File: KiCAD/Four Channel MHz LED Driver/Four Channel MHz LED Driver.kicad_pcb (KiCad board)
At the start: 2 copper layers, 100 x 100 mm, 89 parts, among them J1 Barrel_Jack_Switch, J10 Conn_01x08_Female, J2 Conn_01x02_Female, J3 8P8C_Shielded_x4, J4 Conn_01x05_Female, J5 Conn_01x24_Female, J6 Conn_01x03_Male, J7 Conn_01x24_Female, J8 Conn_01x03_Female, J9 Conn_01x03_Female, M1 Fan_4pin, Q2 SUM70060E, SW1 SW_SPDT, SW2 Pushbutton_with_LED_-_ELUMOAT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, SW3 Pushbutton_with_LED_-_ELUMOAT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, SW4 Pushbutton_with_LED_-_ELUMOAT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, SW5 Pushbutton_with_LED_-_ELUMOAT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, U1 12V boost, U10 LT6200CS8-10, U14 Teensy3.6, U16 SN74LV4T125PWR, U2 ASSR-1218, U3 DPBW06F-05, U4 BDJ0GA5WEFJ-E2, U5 ADP7182AUJZ-1.8-R7, U6 TMUX1204DGSR, U7 ASSR-1218, U8 ASSR-1218, U9 ASSR-1218

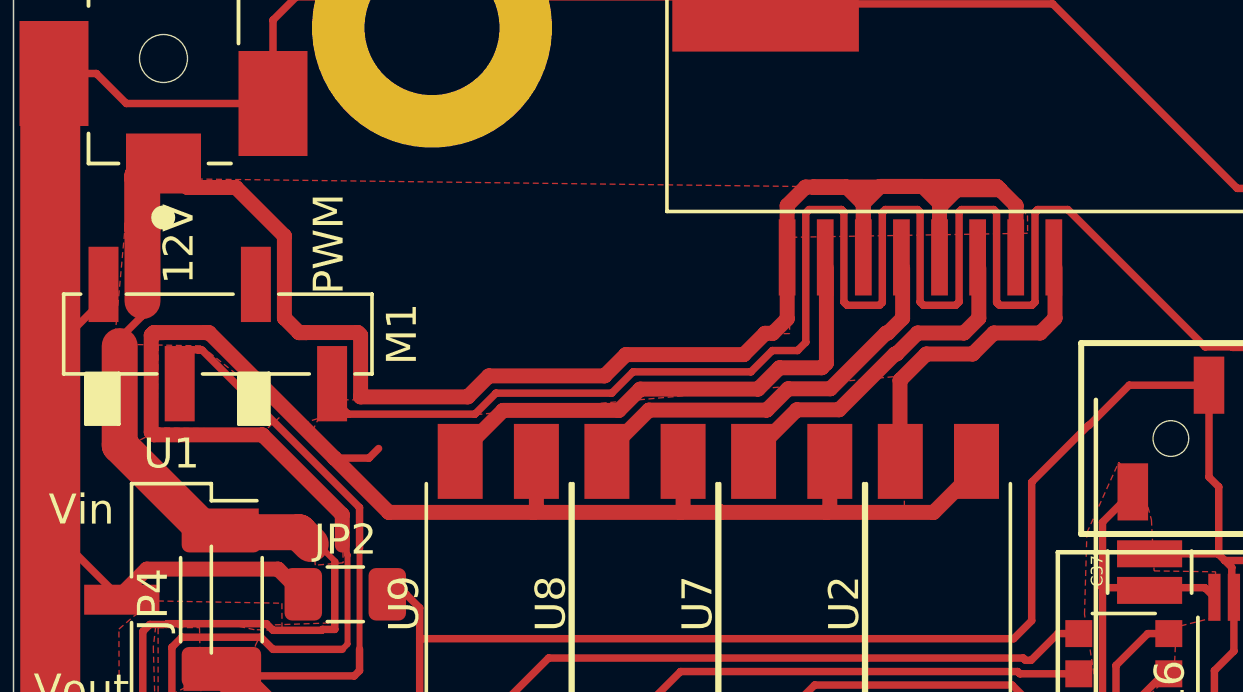
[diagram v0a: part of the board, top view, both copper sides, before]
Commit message: Improved SSR traces to minimize inductance
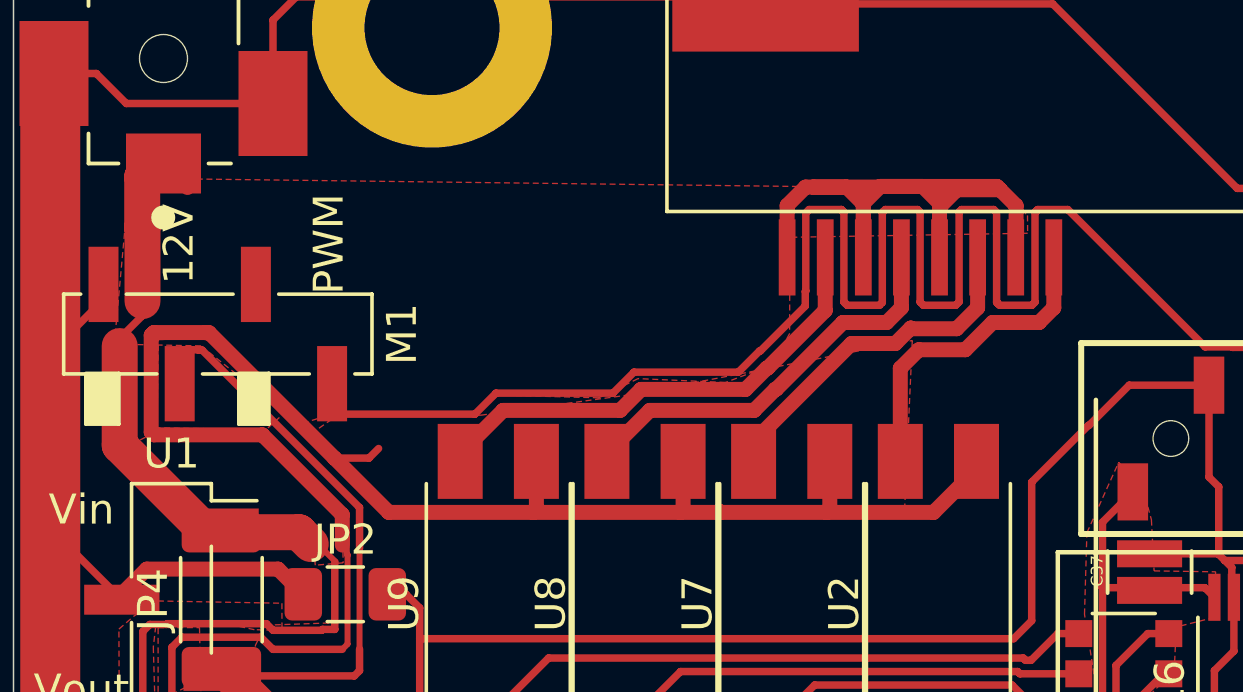
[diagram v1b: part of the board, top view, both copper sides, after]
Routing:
- net /Vin: track 186.8 -> 158.2 mm
- net /LED1-: track 16.9 -> 16.2 mm
- net /5V_fan_PWM: track 70.8 -> 70.2 mm
- net /LED4-: track 10.7 -> 11.2 mm

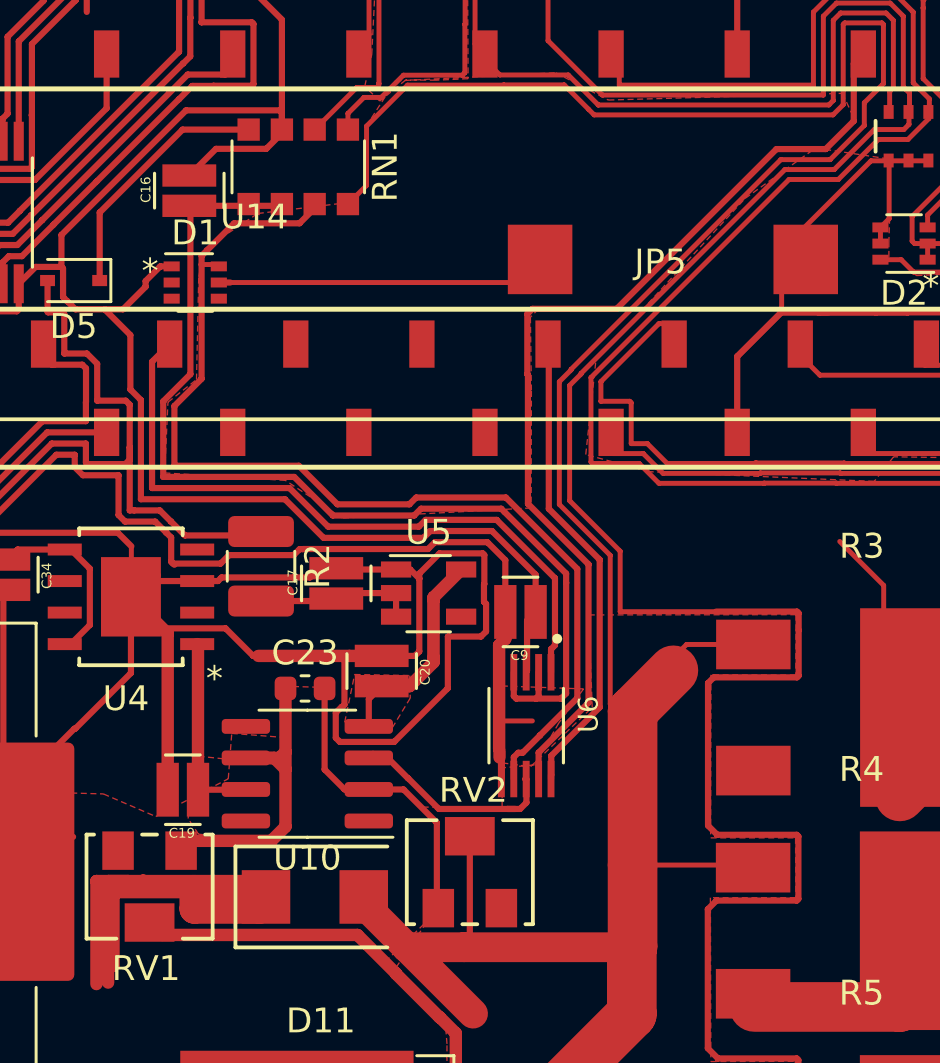
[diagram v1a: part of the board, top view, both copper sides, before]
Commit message: Further refinement of traces to shorter paths with bigger ground pours
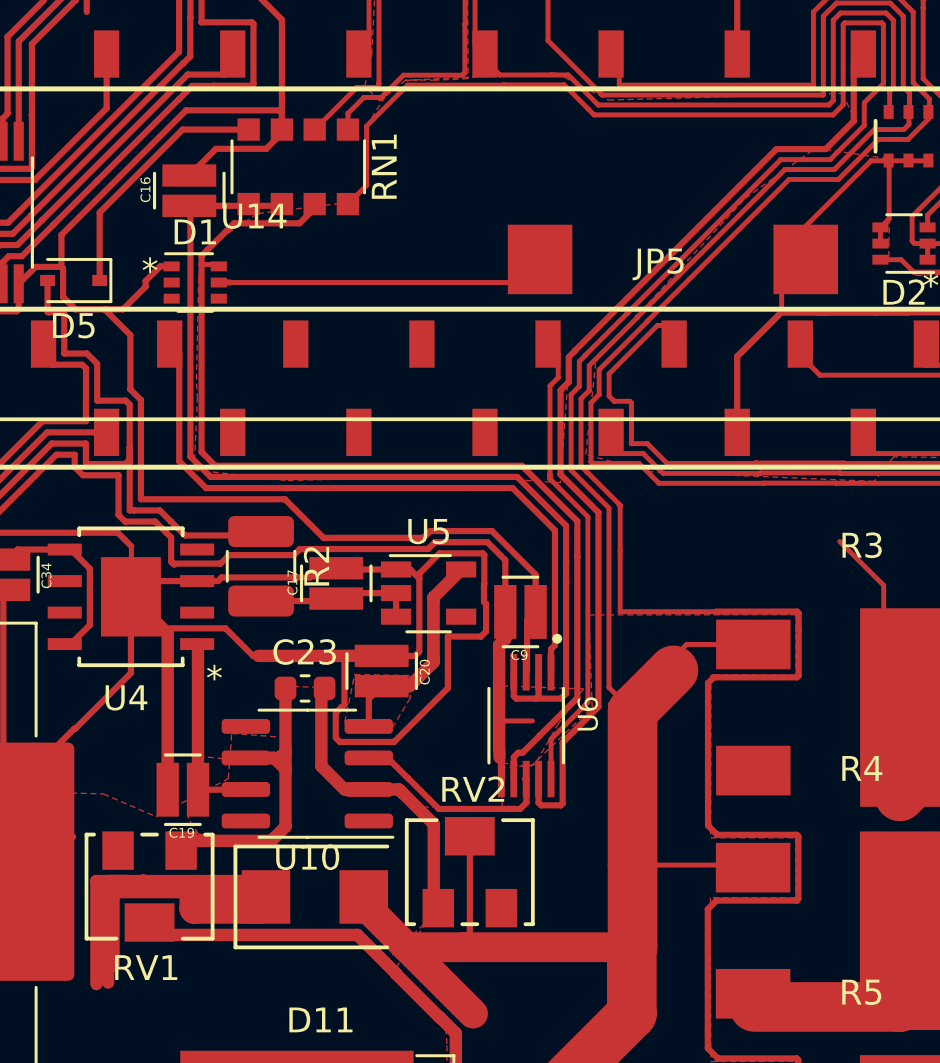
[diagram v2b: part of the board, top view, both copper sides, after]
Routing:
- net /-0.25V_analog: track 42.3 -> 41.2 mm
- net /external_analog: track 43.0 -> 42.0 mm
- net /Interline_PWM: track 27.9 -> 27.1 mm
- net /Toggle_switch: track 173.5 -> 172.8 mm

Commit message: More path optmization
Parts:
- moved RN2 1.53 mm to (128.9, 67.9)
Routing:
- net /Button1: track 127.4 -> 123.9 mm
- net /Over_temp_alarm2: track 83.7 -> 81.5 mm
- net /Resistor_temp: track 98.5 -> 96.3 mm
- net /Toggle_switch: track 172.8 -> 170.6 mm
- net /Button3: track 111.4 -> 109.7 mm
- net /LED1: track 7.74 -> 6.14 mm
- net /3.3V: track 119.2 -> 117.9 mm
- net /Over_temp_alarm1: track 78.2 -> 76.9 mm
- net /LED_pot: track 102.2 -> 100.9 mm
- net /Button2: track 125.5 -> 124.2 mm
- net /Button4: track 91.8 -> 90.6 mm
- net /LED3: track 14.5 -> 13.4 mm
- net /LED2: track 23.8 -> 22.8 mm
- net /LED4: track 6.41 -> 5.85 mm
- added copper zone on F.Cu, net /Button2

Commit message: Organized schematic
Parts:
- moved JP1 0.61 mm to (72.5, 89.6)
- renumbered C14 to C10, C15 to C11, C17 to C12, C34 to C13, C16 to C14, C9 to C15, C37 to C16, C19 to C17, C20 to C18, C12 to C19, C13 to C20, C23 to C21, C5 to C4, C6 to C5, C7 to C6, C10 to C7, C4 to C9, D4 to D3, D11 to D4, R5 to R1, R1 to R2, R2 to R5
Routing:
- net /LED-: track 161.8 -> 168.9 mm
- net /Vin: track 158.2 -> 161.9 mm
- net /-5V: track 45.6 -> 43.6 mm
- net /12V: track 68.8 -> 67.3 mm
- net /5V: track 107.3 -> 106.4 mm
- net /Relay3: track 33.4 -> 34.1 mm
- net /Relay4: track 32.3 -> 32.8 mm
- net Net-(J3-Pad21): track 15.7 -> 15.2 mm

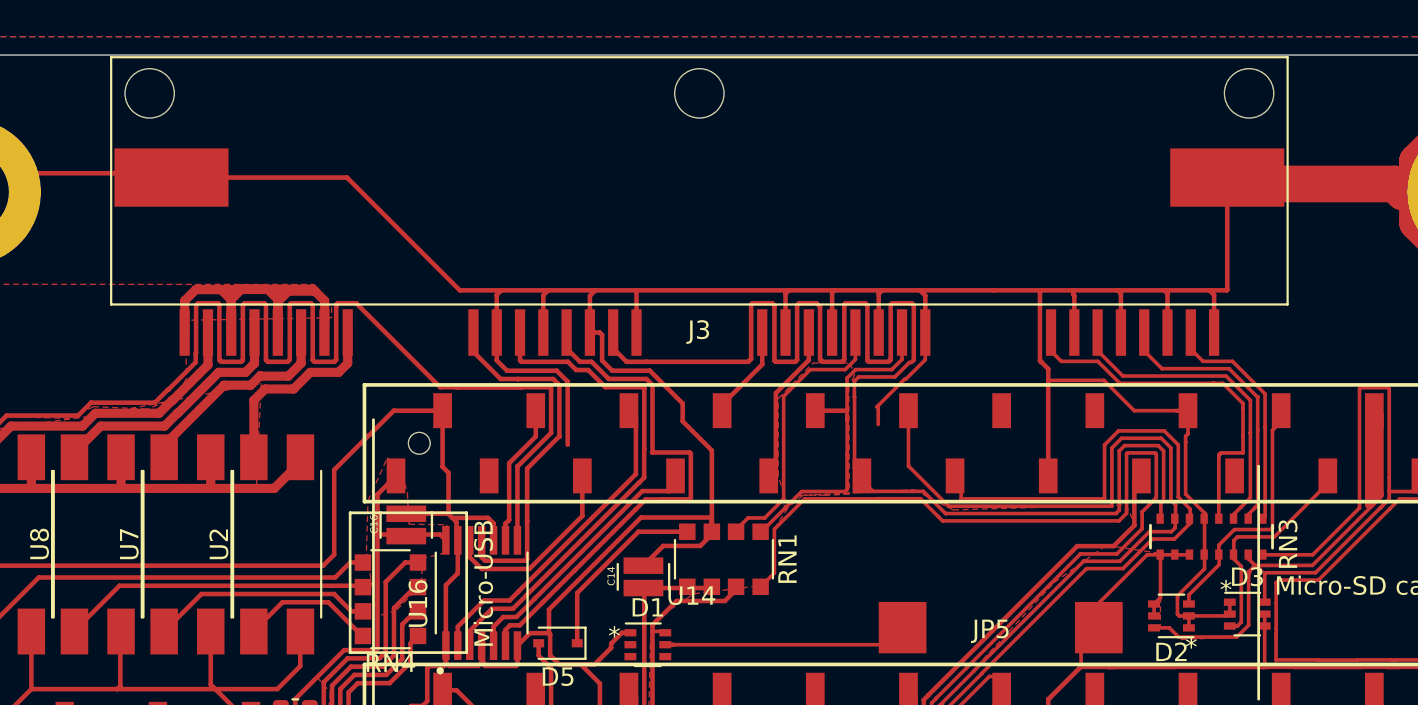
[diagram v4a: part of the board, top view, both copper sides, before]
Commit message: Fix PCB after cleaned up schematic
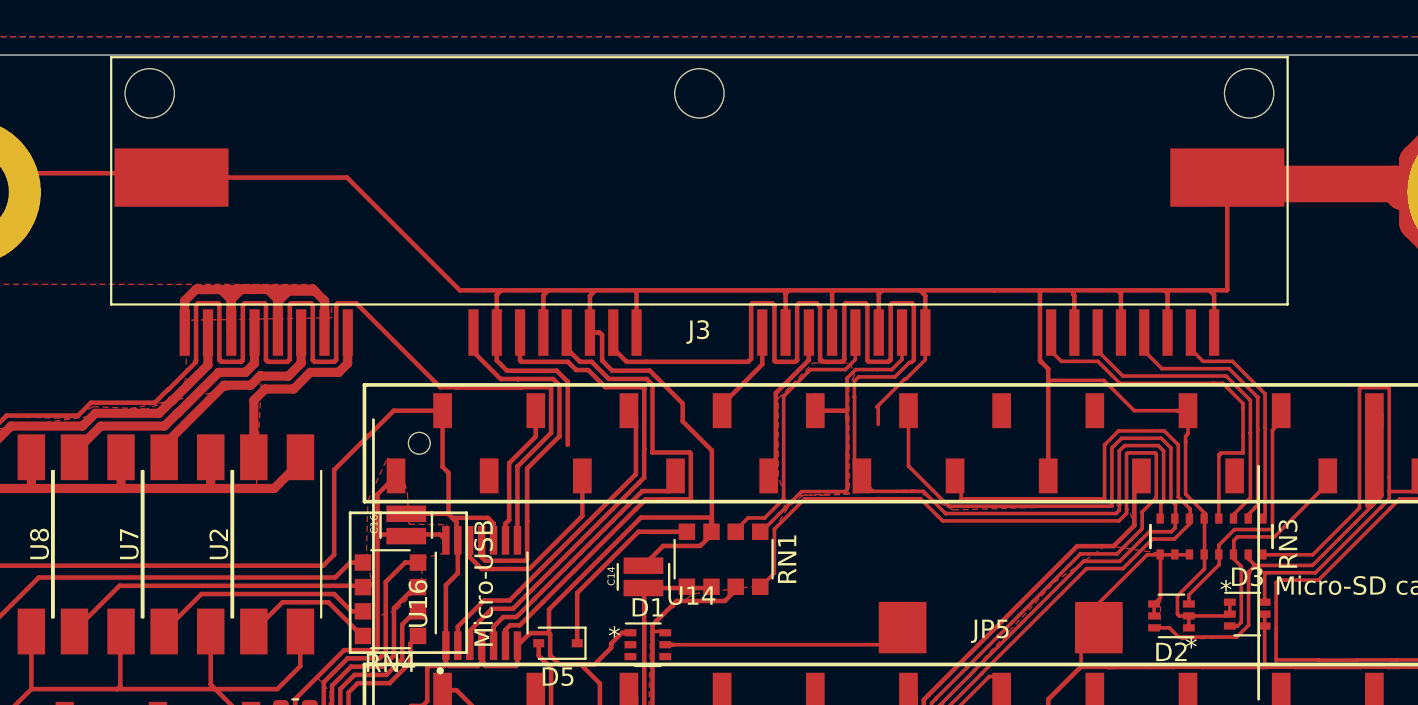
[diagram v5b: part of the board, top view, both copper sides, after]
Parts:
- SW2, SW3, SW4, SW5: value Pushbutton_with_LED_-_ELUMOATHQ3C12 -> Pushbutton_with_LED

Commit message: Re-annotate DRC pass
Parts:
- renumbered C7 to C1, C9 to C10, C19 to C11, C20 to C12, C10 to C13, C11 to C14, C14 to C15, C15 to C16, C12 to C17, C13 to C18, C17 to C19, C1 to C2, C18 to C20, C2 to C3, C3 to C4, C4 to C5, C5 to C6, C6 to C7, C16 to C9, D5 to D4, D4 to D5, H2 to H1, H3 to H2, H1 to H3, H14 to H5, H15 to H6, H16 to H7, H17 to H8, J7 to J10, J6 to J4, J9 to J5, J10 to J6, J8 to J7, J4 to J8, J5 to J9, JP4 to JP2, JP2 to JP3, JP5 to JP4, JP3 to JP5, Q2 to Q1, R5 to R1, R6 to R2, R1 to R3, R2 to R4, R3 to R5, R4 to R6, RN2 to RN1, RN1 to RN2, RV3 to RV1, RV1 to RV2, RV2 to RV3, SW2 to SW1, SW3 to SW2, SW4 to SW3, SW1 to SW4, U8 to U10, U9 to U11, U14 to U12, U16 to U2, U6 to U4, U4 to U5, U5 to U6, U10 to U7, U2 to U8, U7 to U9

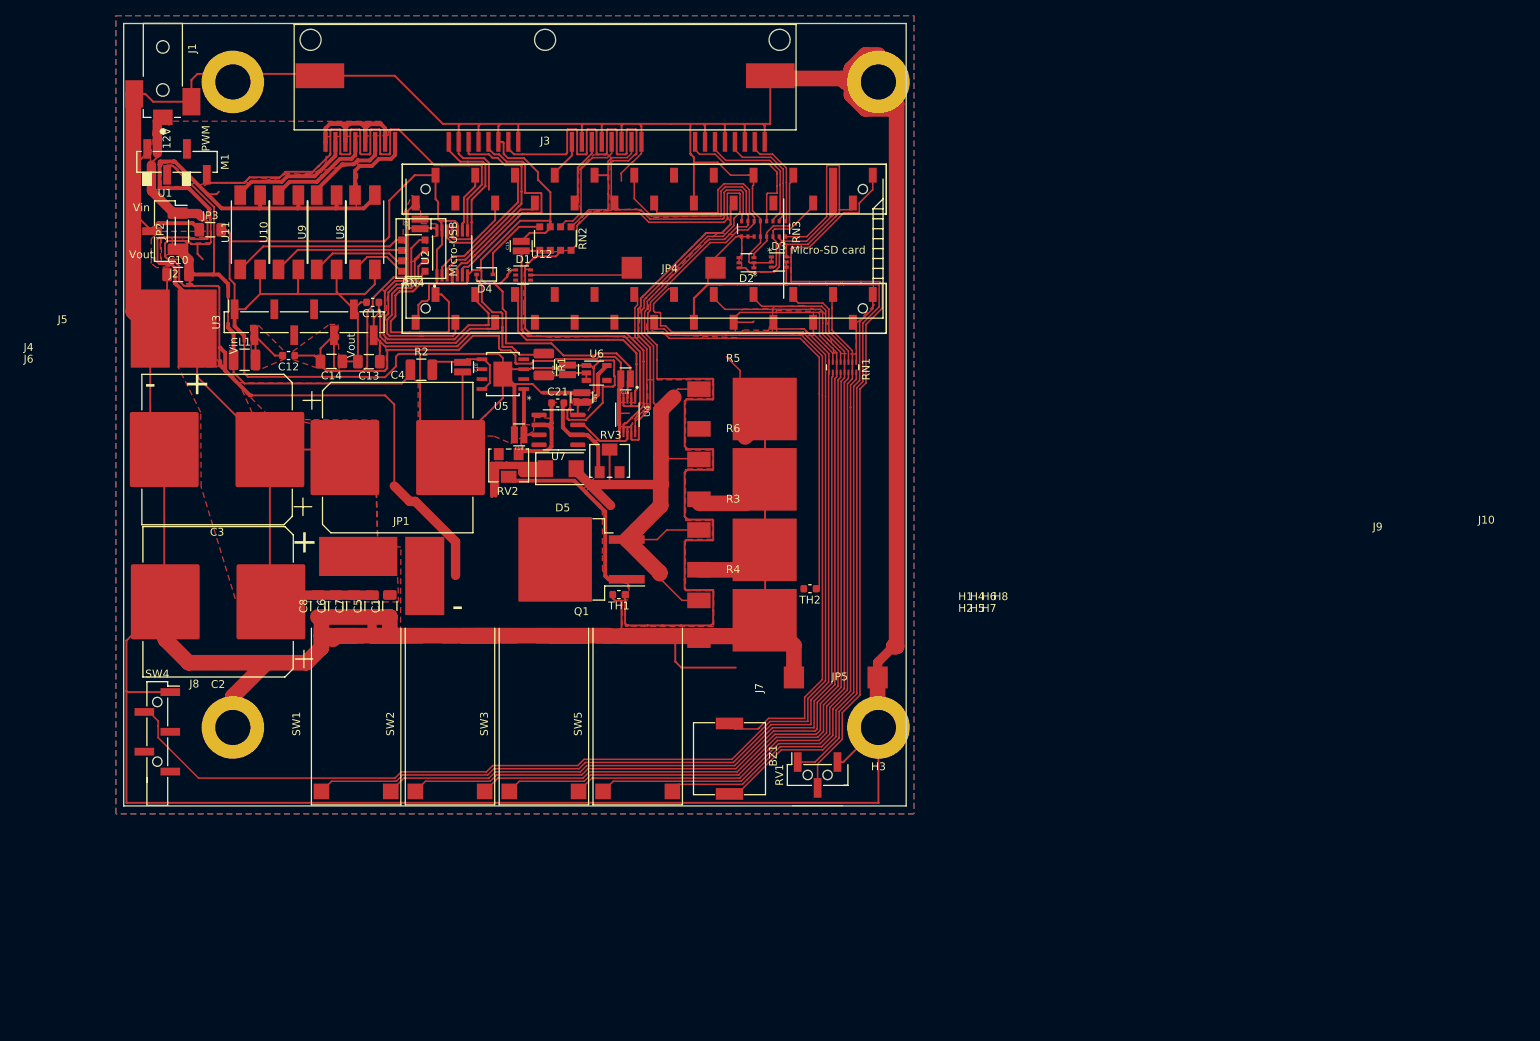
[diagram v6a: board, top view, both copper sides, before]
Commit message: Fix footprints and position silkscreen labels
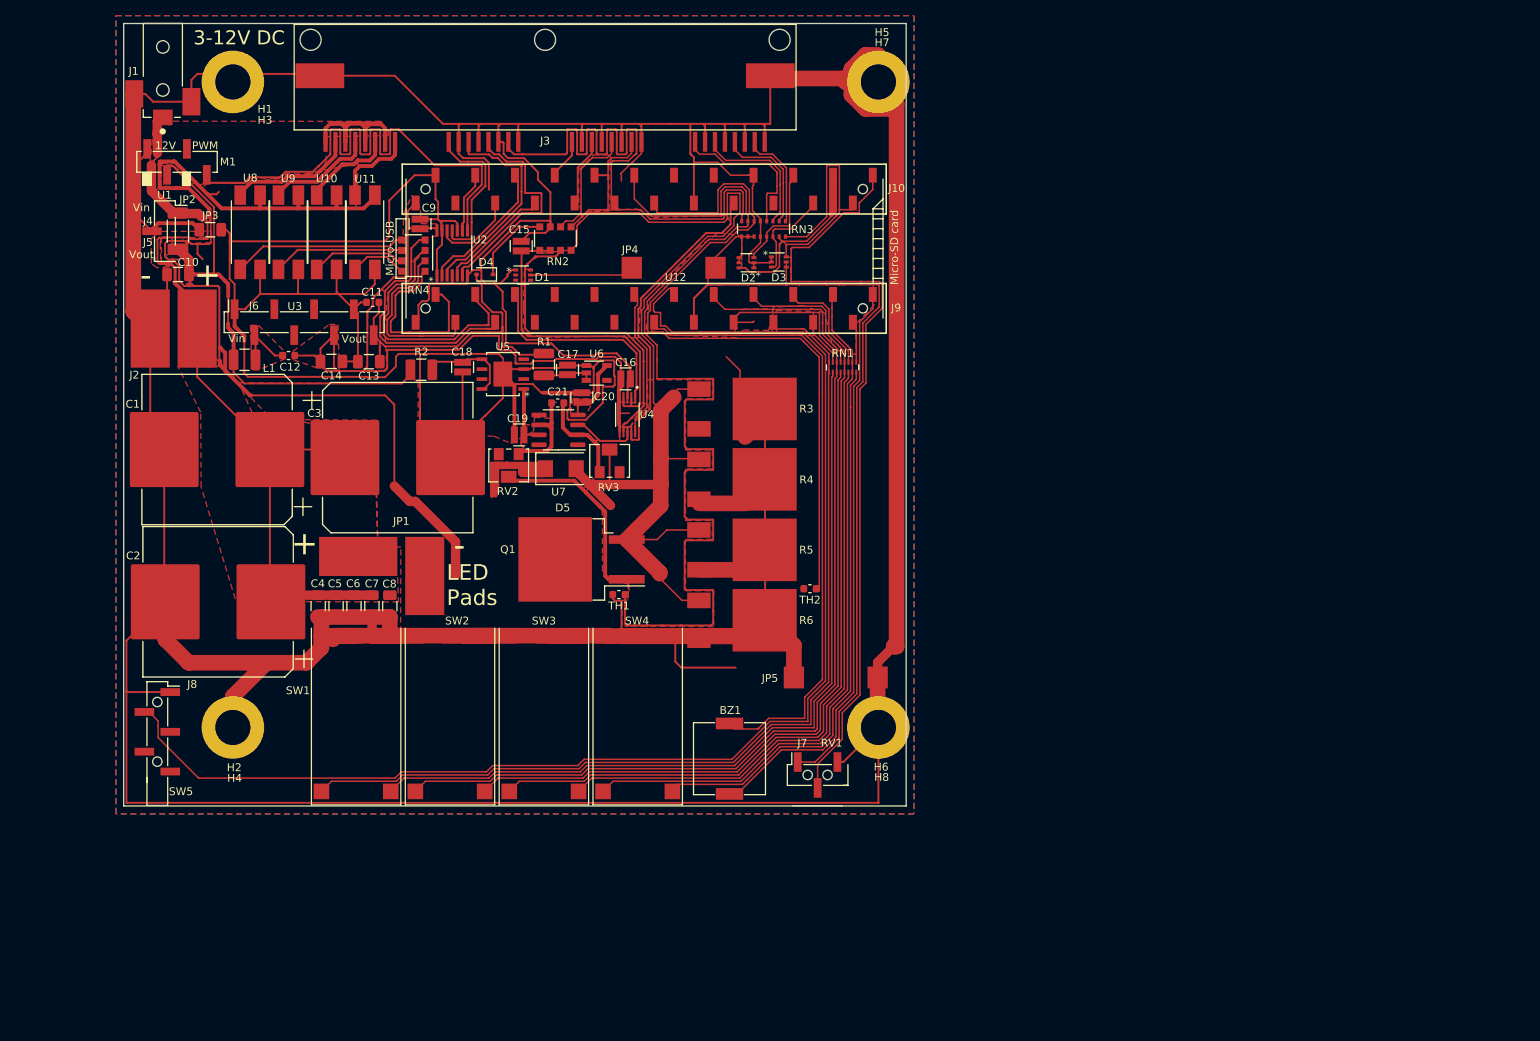
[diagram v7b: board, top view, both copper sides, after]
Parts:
- U5: value BDJ0GA5WEFJ-E2 -> HTSOP-J8_ROM
- moved C7 6.91 mm to (68.7, 98.5)
- moved C4 6.89 mm to (61.9, 98.5)
- renumbered C3 to C1, C4 to C3, C5 to C4, C6 to C5, C7 to C6, C8 to C7, C1 to C8, R5 to R3, R6 to R4, R3 to R5, R4 to R6, SW5 to SW4, SW4 to SW5, U9 to U10, U8 to U11, U11 to U8, U10 to U9
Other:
- board text added: "3-12V DC"
- board text added: "LED Pads"
